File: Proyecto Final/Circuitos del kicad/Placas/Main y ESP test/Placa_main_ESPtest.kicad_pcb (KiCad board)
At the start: 2 copper layers, 118.7 x 100 mm, 21 parts, among them J1 12v, J2 Conn_02x05_Odd_Even, J3 Conn_02x06_Odd_Even, J4 Conn_01x08, J5 Conn_01x08, J6 Conn_01x06, U1 LM7805, U2 ESP-12E, U3 ATmega328P-P, U4 LM1117-3.3, U5 BOB-12009, Y1 16MHz

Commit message: Agrandado de pistas y cambio en agujeros
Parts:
- removed the R1 at (132.0, 78.0)
- added C7: 100nF, Capacitor_THT:C_Disc_D5.0mm_W2.5mm_P5.00mm, F.Cu at (145.5, 93.8)
- added R2: 10k, Resistor_THT:R_Axial_DIN0204_L3.6mm_D1.6mm_P5.08mm_Horizontal, F.Cu at (132.2, 78.1)
- U4: moved to B.Cu
- moved RTC+LCD1 2.36 mm to (151.5, 70.1)
- moved C3 0.66 mm to (145.8, 116.0)
- moved U4 0.20 mm to (136.9, 67.8)
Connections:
- U3 pad 1: unconnected-(U3-Pad1) -> Net-(R2-Pad1)
- U3 pad 21: unconnected-(U3-Pad21) -> Net-(U3-Pad21)
- U4 pad 1: +5V -> GND
- U4 pad 3: GND -> +5V
- U4 pad 4: Net-(C6-Pad1) -> (no net)
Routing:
- net Net-(J3-Pad7): track 146.1 -> 160.2 mm
- net Net-(U3-Pad21): track 0.00 -> 5.76 mm
- net +5V: track 203.9 -> 209.4 mm
- net Net-(J3-Pad6): track 41.7 -> 36.6 mm
- net Net-(J3-Pad8): track 40.6 -> 36.1 mm
- net Net-(J3-Pad10): track 38.7 -> 34.7 mm
- net unconnected-(U3-Pad1): track 2.85 -> 0.00 mm
- net GND: track 315.2 -> 318.0 mm
- net Net-(R2-Pad1): track 0.00 -> 2.67 mm
- net Net-(J4-Pad1): track 100.5 -> 102.2 mm
- net Net-(J5-Pad2): track 20.4 -> 21.5 mm
- net +12V: track 68.0 -> 66.9 mm
- net Net-(RTC+LCD1-Pad3): track 13.9 -> 14.8 mm
- net Net-(RTC+LCD1-Pad1): track 13.9 -> 14.8 mm
- net Net-(U3-Pad3): track 35.9 -> 36.6 mm
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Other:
- outline, holes or cut-outs redrawn

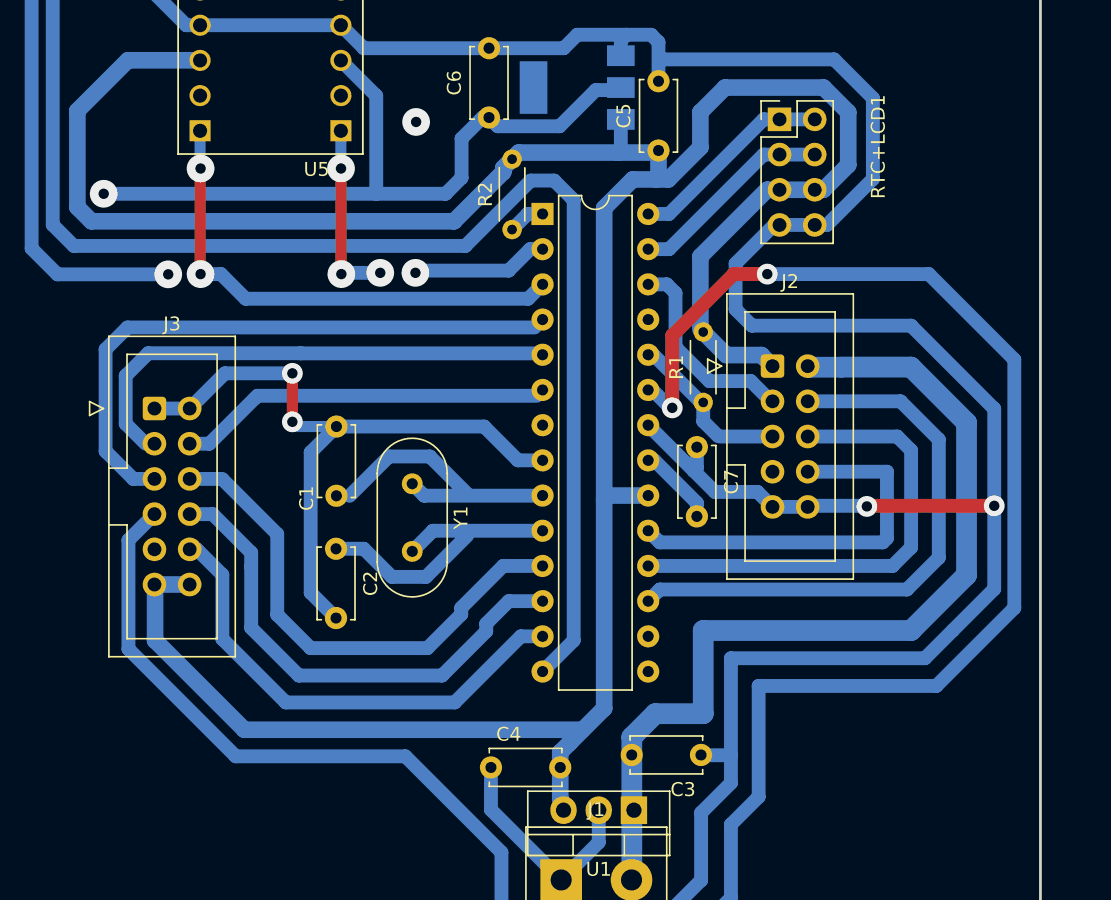
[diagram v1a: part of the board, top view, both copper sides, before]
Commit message: Puse ambas masas por las dudas
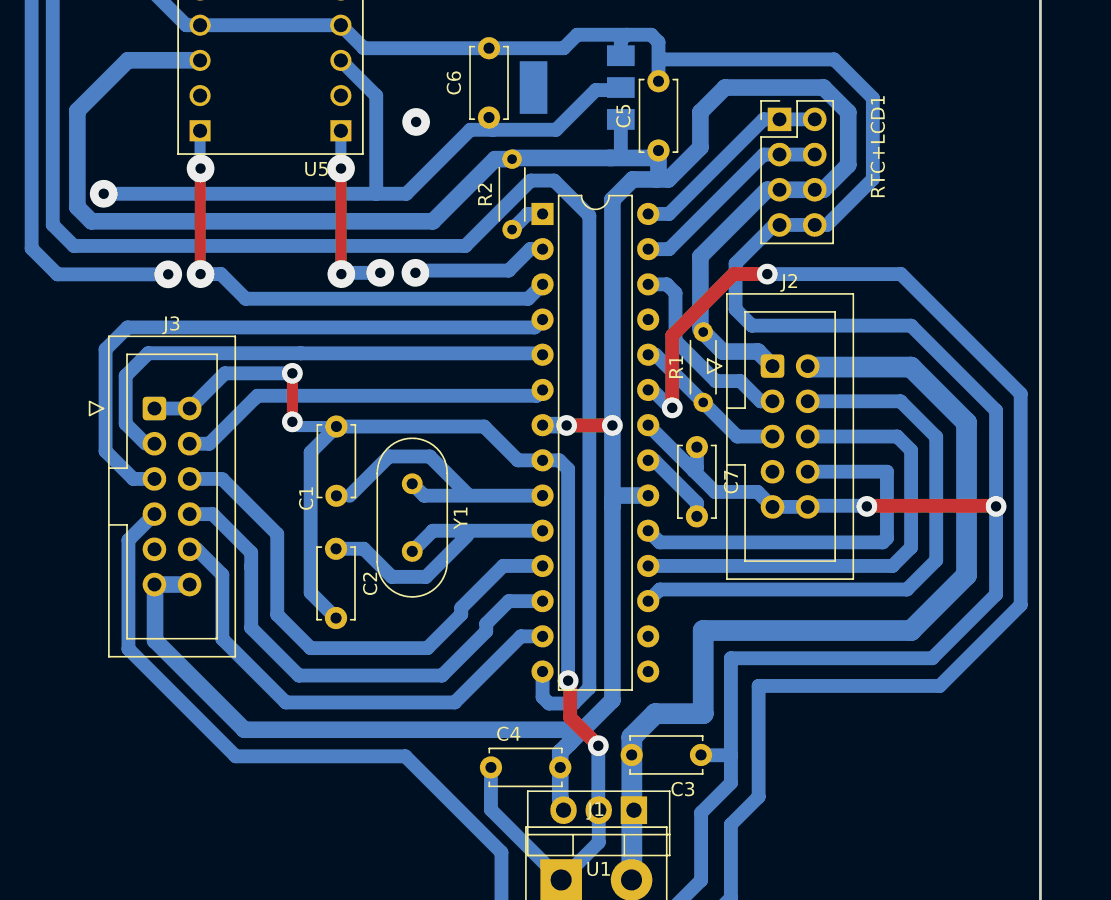
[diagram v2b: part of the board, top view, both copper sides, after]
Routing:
- net GND: track 318.0 -> 346.2 mm, vias 5 -> 7
- net Net-(J4-Pad1): track 102.2 -> 108.8 mm
- net +5V: track 209.4 -> 213.9 mm, vias 0 -> 2
- net Net-(C6-Pad1): track 53.7 -> 52.2 mm
- net Net-(J3-Pad7): track 160.2 -> 159.5 mm
- net Net-(J2-Pad3): track 14.9 -> 14.4 mm

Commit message: a
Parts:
- removed C7: 100nF, Capacitor_THT:C_Disc_D5.0mm_W2.5mm_P5.00mm
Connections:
- J2 pad 1: +5V -> GND
- J2 pad 10: GND -> +12V
- J2 pad 2: +12V -> GND
- J2 pad 8: Net-(J2-Pad8) -> Net-(U3-Pad21)
- J2 pad 9: GND -> +5V
- U3 pad 19: Net-(J2-Pad8) -> Net-(U3-Pad21)
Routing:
- net Net-(U3-Pad21): track 5.76 -> 34.1 mm
- net Net-(J2-Pad8): track 28.3 -> 0.00 mm
- net GND: track 346.2 -> 325.2 mm, vias 7 -> 5
- net +12V: track 67.1 -> 47.6 mm, vias 0 -> 2
- net Net-(J2-Pad4): track 41.2 -> 47.6 mm
- net Net-(J3-Pad7): track 159.5 -> 165.6 mm
- net Net-(J2-Pad6): track 34.8 -> 40.7 mm
- net +5V: track 213.9 -> 217.2 mm
- net Net-(J2-Pad3): track 14.4 -> 15.3 mm
- net Net-(J2-Pad5): track 11.6 -> 12.2 mm

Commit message: a
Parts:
- added REF**: CP_Radial_D6.3mm_P2.50mm, Capacitor_THT:CP_Radial_D6.3mm_P2.50mm, F.Cu at (145.0, 95.0)
- moved R1 2.05 mm to (148.0, 91.0)
- moved J2 2.00 mm to (153.0, 87.9)
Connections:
- J3 pad 7: Net-(J3-Pad7) -> Net-(J2-Pad5)
- U3 pad 23: Net-(J3-Pad7) -> Net-(J2-Pad5)
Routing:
- net Net-(J3-Pad7): track 165.6 -> 0.00 mm, vias 2 -> 0
- net Net-(J2-Pad5): track 12.2 -> 172.6 mm, vias 0 -> 2
- net Net-(J2-Pad4): track 47.6 -> 43.3 mm
- net Net-(J2-Pad6): track 40.7 -> 36.4 mm
- net +5V: track 217.2 -> 220.4 mm
- net GND: track 325.2 -> 326.4 mm
- net Net-(U3-Pad21): track 34.1 -> 33.1 mm
- net +12V: track 47.6 -> 48.3 mm
- net Net-(J2-Pad3): track 15.3 -> 16.0 mm
